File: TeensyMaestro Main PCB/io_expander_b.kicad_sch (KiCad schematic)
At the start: 29 parts, among them J3 Male Connector, J4 B5B-XH-A_LF__SN_, SW10 PEC11L-4120F-S0020, SW6 RotaryEncoder_Powered, SW7 PEC11L-4120F-S0020, SW8 PEC11L-4120F-S0020, SW9 PEC11L-4120F-S0020, U5 MCP23008-xP

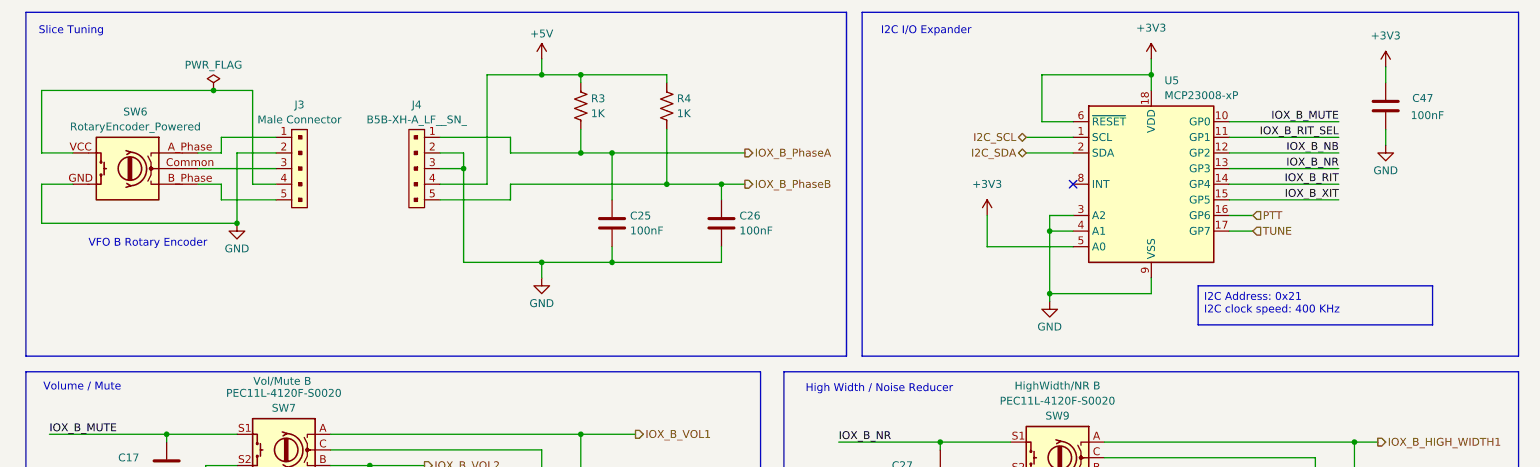
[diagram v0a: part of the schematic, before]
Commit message: Updated documentation in schematic
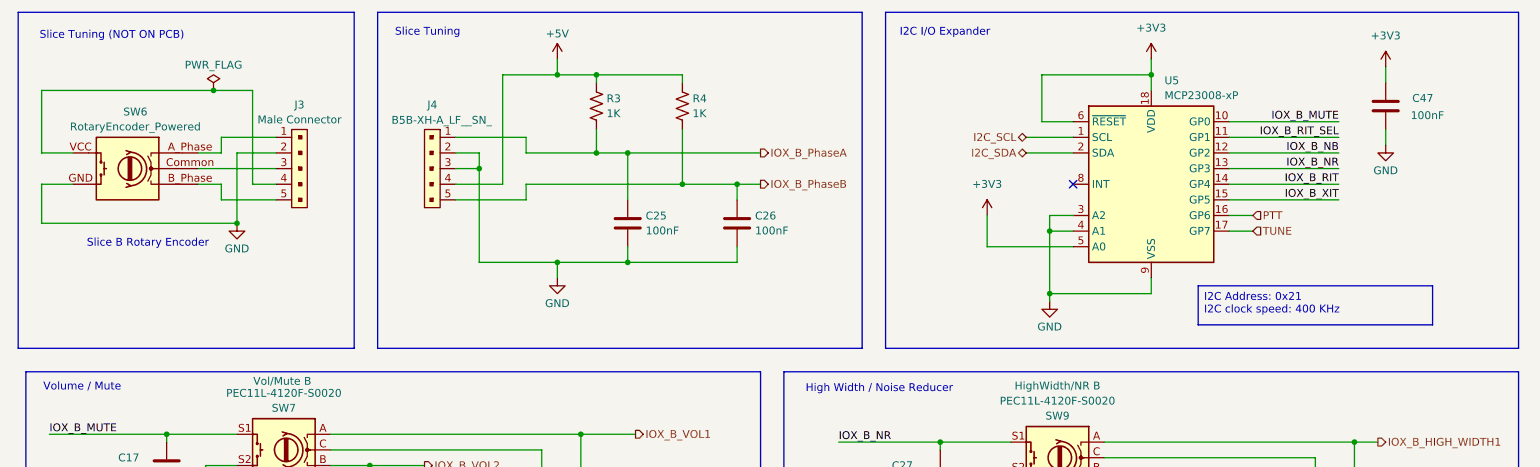
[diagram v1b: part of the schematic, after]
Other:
- note added: "Slice B Rotary Encoder"
- note added: "Slice Tuning (NOT ON PCB)"
- note removed: "VFO B Rotary Encoder"
- moved on the sheet: C25, C26, J4, R3, R4

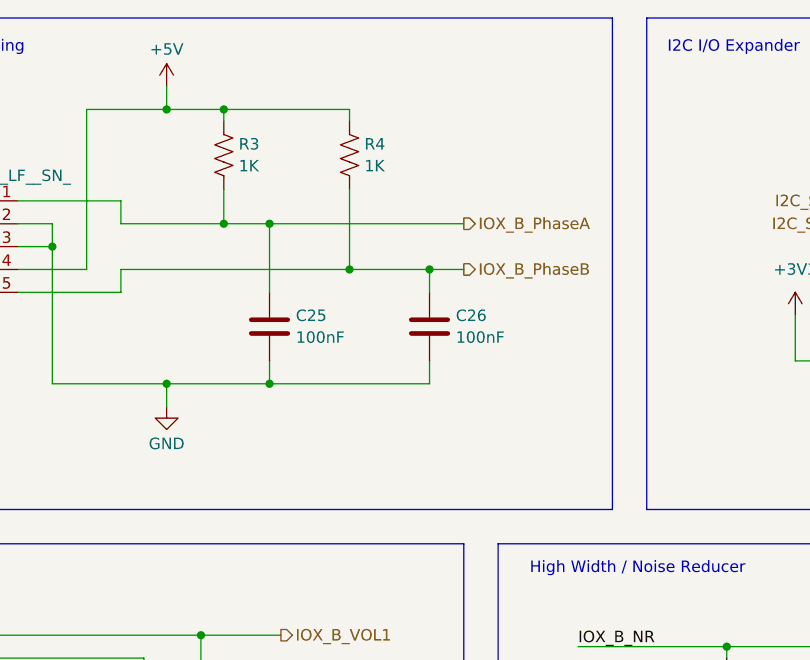
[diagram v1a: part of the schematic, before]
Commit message: Update schematic with 5v pullup correction
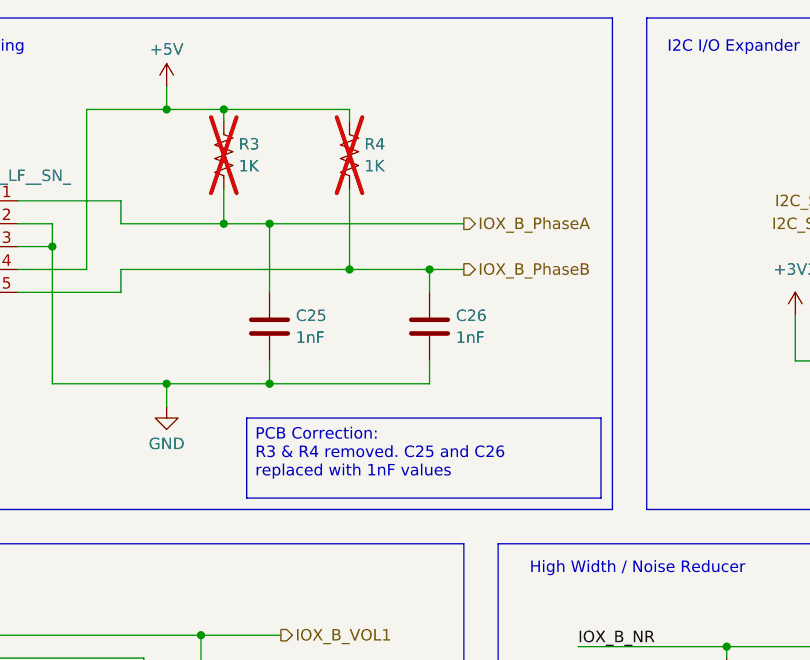
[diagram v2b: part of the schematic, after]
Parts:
- C25, C26: value 100nF -> 1nF
- R3: now not fitted; now left out of the parts list
- R4: now not fitted
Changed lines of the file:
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@@
 		)
 	)
+	(text_box "PCB Correction:\nR3 & R4 removed. C25 and C26 replaced with 1nF values"
+		(exclude_from_sim no)
+		(at 111.76 60.96 0)
+		(size 39.37 8.89)
+		(margins 0.9525 0.9525 0.9525 0.9525)
+		(stroke
+			(width 0)
+			(type solid)
+		)
+		(fill
+			(type none)
+		)
+		(effects
+			(font
+				(size 1.27 1.27)
+			)
+			(justify left top)
+		)
+	)
 	(text_box "I2C Address: 0x21\nI2C clock speed: 400 KHz"
 		(exclude_from_sim no)
@@
 		(at 123.19 31.75 0)
 		(unit 1)
-		(exclude_from_sim no)
+		(exclude_from_sim yes)
 		(in_bom yes)
-		(on_board yes)
-		(dnp no)
+		(on_board no)
+		(dnp yes)
 		(fields_autoplaced yes)
 		(property "Reference" "R4"
@@
 			)
 		)
-		(property "Value" "100nF"
+		(property "Value" "1nF"
 			(at 135.001 52.0121 0)
 			(effects
@@
 			)
 		)
-		(property "Value" "100nF"
+		(property "Value" "1nF"
 			(at 117.221 52.0121 0)
 			(effects
@@
 		(at 109.22 31.75 0)
 		(unit 1)
-		(exclude_from_sim no)
-		(in_bom yes)
+		(exclude_from_sim yes)
+		(in_bom no)
 		(on_board yes)
-		(dnp no)
+		(dnp yes)
 		(fields_autoplaced yes)
 		(property "Reference" "R3"

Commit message: Update schematic & BOM with 5v pullup correction
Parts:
- R4: now left out of the parts list
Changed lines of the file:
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@@
 		(unit 1)
 		(exclude_from_sim yes)
-		(in_bom yes)
-		(on_board no)
+		(in_bom no)
+		(on_board yes)
 		(dnp yes)
 		(fields_autoplaced yes)
